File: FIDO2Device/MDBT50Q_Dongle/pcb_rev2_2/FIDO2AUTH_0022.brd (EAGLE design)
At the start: 19.5 x 34.3 mm, 40 parts, among them CN1 TE-1734028, CN2 IF_5PIN_H, SW1 SKRPACE010, SW2 SKTADAE010, U1 MDBT50Q-P1M, U2 XC6206P302MR-G, U4 RV-3028-C7, X1 NX3215SA-32.768K

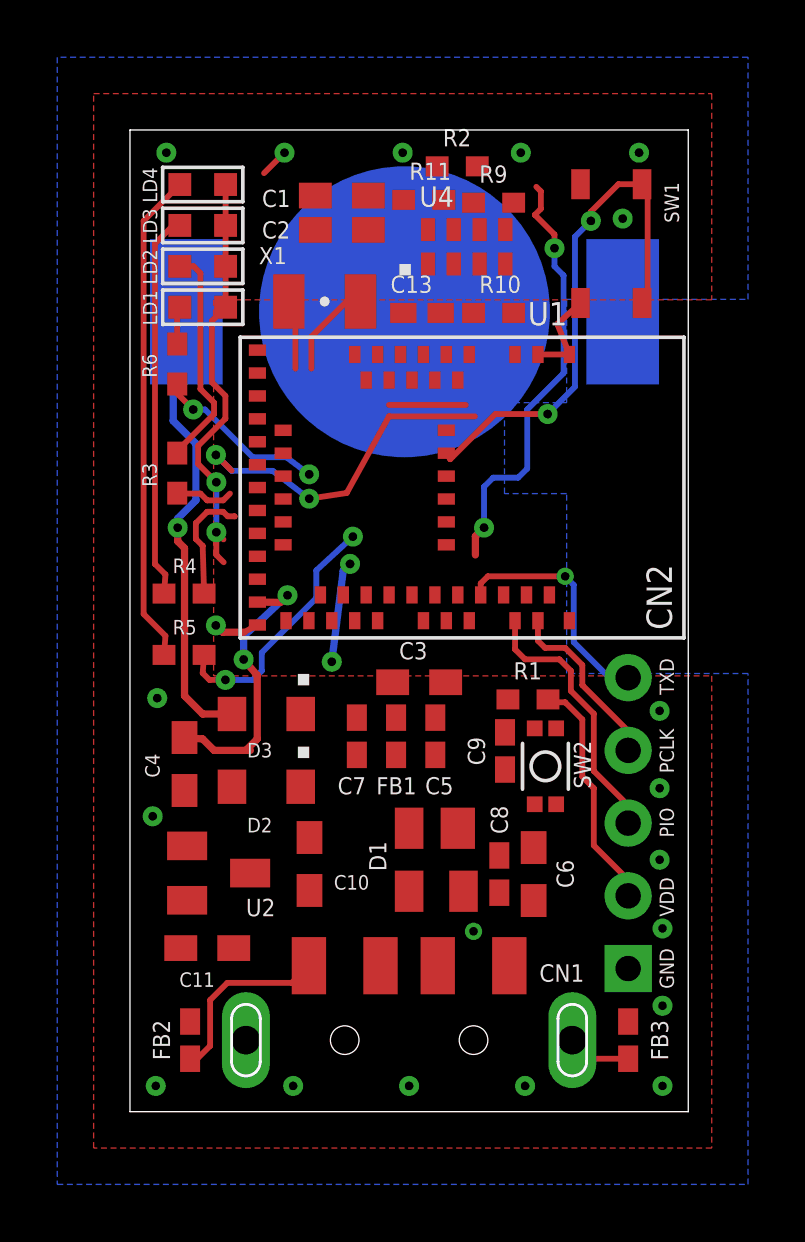
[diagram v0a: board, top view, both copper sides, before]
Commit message: 配線レイアウトを作成
・LED／RTCC／クリスタルを仮配置・配線
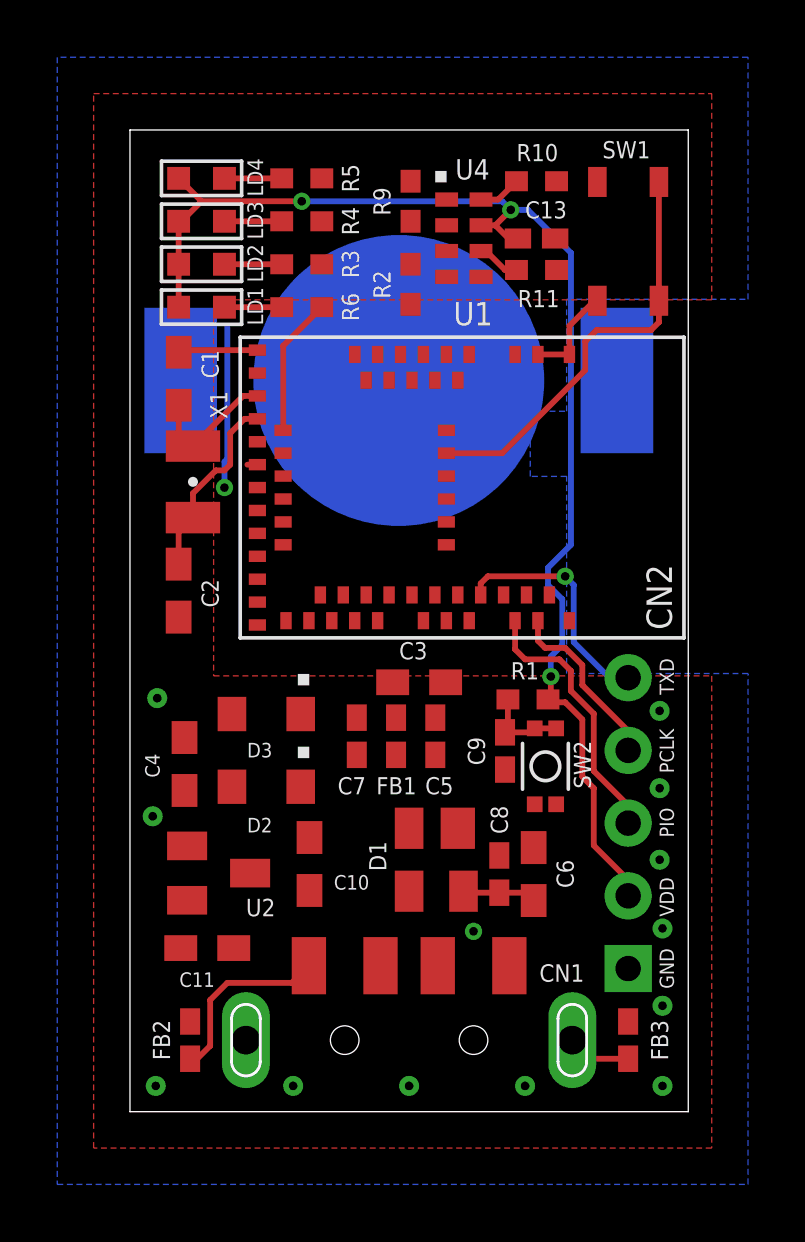
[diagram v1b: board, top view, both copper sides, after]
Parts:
- moved R5 17.1 mm to (6.00, 32.6)
- moved C2 13.8 mm to (1.70, 18.2), turned to 270 degrees
- moved R4 13.6 mm to (6.00, 31.1)
- moved C1 8.57 mm to (1.70, 25.6), turned to 90 degrees
- moved R3 8.49 mm to (6.00, 29.6), turned to 180 degrees
- moved X1 7.80 mm to (2.20, 22.0), turned to 270 degrees
- moved R10 4.84 mm to (14.2, 32.5), turned to 180 degrees
- moved R6 4.78 mm to (6.00, 28.1), turned to 180 degrees
- moved C13 4.77 mm to (14.2, 30.5)
- moved R11 4.64 mm to (14.2, 29.4), turned to 180 degrees
- moved R2 4.43 mm to (9.80, 28.9), turned to 270 degrees
- moved U4 2.94 mm to (10.7, 32.1), turned to 270 degrees
- moved R9 2.90 mm to (9.80, 31.8), turned to 90 degrees
- moved BAT1 2.41 mm to (9.39, 25.5)
- moved SW1 0.59 mm to (17.4, 30.4)
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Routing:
- net N$1: track 17.3 -> 2.00 mm
- net N$5: track 16.6 -> 2.10 mm, vias 1 -> 0
- net N$6: track 13.5 -> 2.00 mm
- net VBUS_NRF: track 10.0 -> 0.00 mm, vias 2 -> 0
- net LED4: track 8.97 -> 0.00 mm, vias 2 -> 0
- net TWI_SDA: track 12.0 -> 5.99 mm, vias 2 -> 1
- net N$7: track 7.83 -> 2.00 mm
- net LED3: track 4.15 -> 0.00 mm
- net SW1: track 18.5 -> 14.8 mm, vias 2 -> 0
- net VDD_NRF: track 42.4 -> 45.8 mm, vias 6 -> 3
- net XL2: track 3.35 -> 6.65 mm
- net RESET: track 0.00 -> 3.04 mm
- net TWI_SCL: track 2.68 -> 0.00 mm
- net VBUS: track 0.00 -> 2.58 mm
- net LED2: track 2.04 -> 0.00 mm
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
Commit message: 配線レイアウトを作成
・VBUS周りを配線
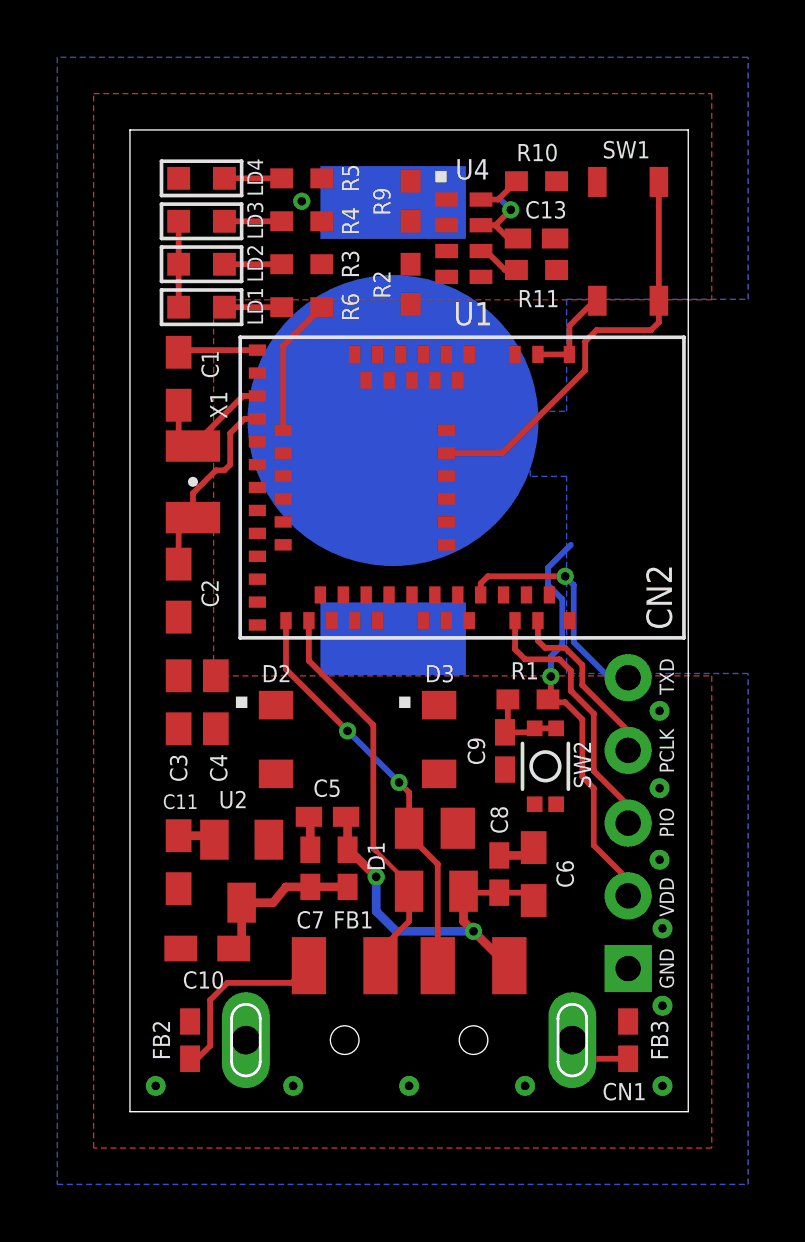
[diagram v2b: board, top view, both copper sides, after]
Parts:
- moved C3 8.43 mm to (1.70, 14.3), turned to 270 degrees
- moved D3 6.10 mm to (10.8, 13.0), turned to 270 degrees
- moved FB1 4.91 mm to (7.60, 8.50)
- moved C7 4.89 mm to (6.30, 8.50)
- moved C5 4.70 mm to (6.90, 10.3), turned to 180 degrees
- moved C10 4.63 mm to (2.70, 5.70), turned to 180 degrees
- moved C11 3.16 mm to (1.70, 8.71), turned to 270 degrees
- moved C4 2.42 mm to (3.00, 14.3)
- moved D2 1.68 mm to (5.10, 13.0), turned to 270 degrees
- moved BAT1 1.41 mm to (9.19, 24.1), turned to 90 degrees
- moved U2 0.81 mm to (3.90, 8.40), turned to 180 degrees
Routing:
- net VDD_NRF: track 45.8 -> 20.2 mm
- net D_N: track 0.00 -> 14.2 mm, vias 0 -> 2
- net D_P: track 0.00 -> 13.9 mm
- net VBUS: track 2.58 -> 13.3 mm, vias 1 -> 2
- net TWI_SDA: track 5.99 -> 0.00 mm, vias 1 -> 0
- net VBUS_NRF: track 0.00 -> 5.67 mm
- net 0V: track 6.22 -> 8.70 mm, vias 12 -> 10
- net N$5: track 2.10 -> 0.00 mm
- net N$4: track 0.00 -> 1.31 mm

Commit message: 配線レイアウトを作成
・VDD_NRF周りを配線
・RESET配線を修正
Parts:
- moved R1 0.10 mm to (13.8, 14.4)
- turned BAT1 to 270 degrees
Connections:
- net N$5: now also BAT1.+@2; no longer BAT1.+@1
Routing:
- net VDD_NRF: track 20.2 -> 66.7 mm, vias 3 -> 7
- net RESET: track 3.04 -> 16.5 mm, vias 0 -> 2
- net N$5: track 0.00 -> 5.97 mm, vias 0 -> 1
- net VBUS_NRF: track 5.67 -> 9.11 mm
- net 0V: track 8.70 -> 9.75 mm, vias 10 -> 11

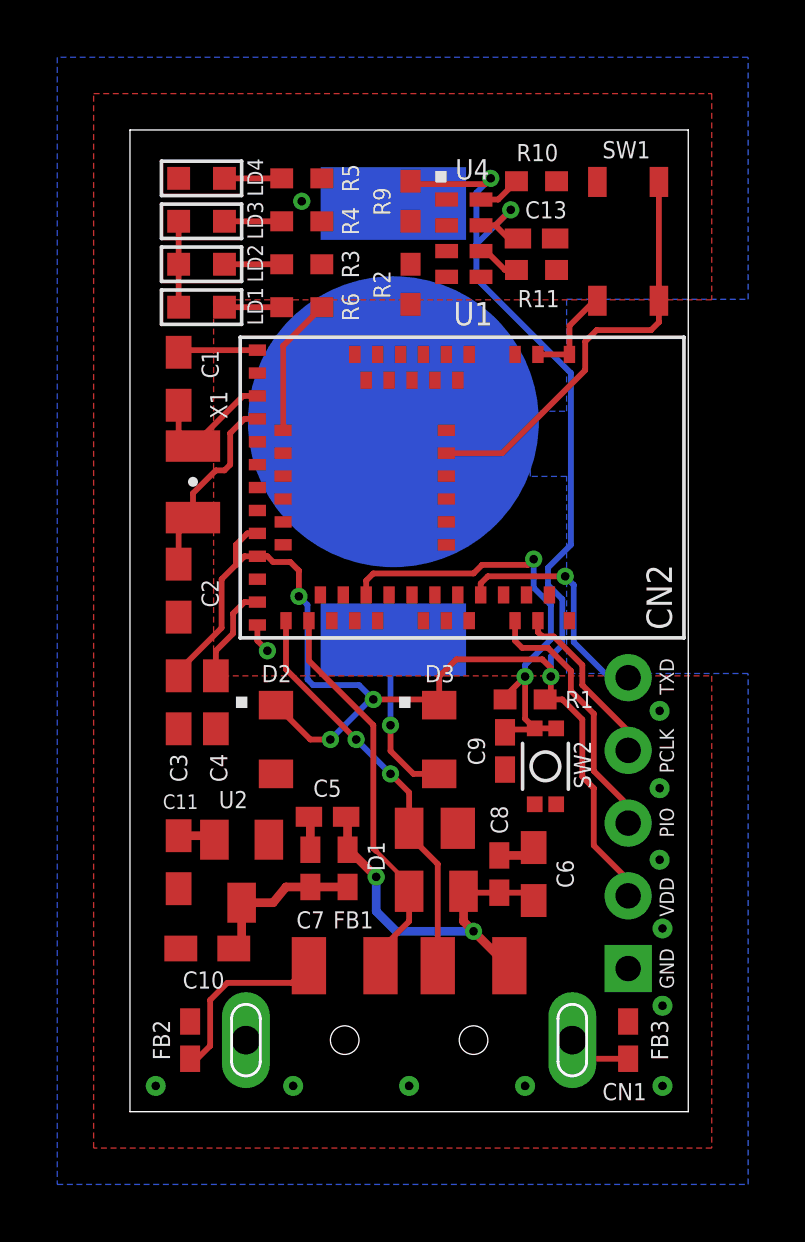
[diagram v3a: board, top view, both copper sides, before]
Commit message: 配線レイアウトを作成
・基板下半分のVDD_NRF、VBUS_NRFの配線を確定
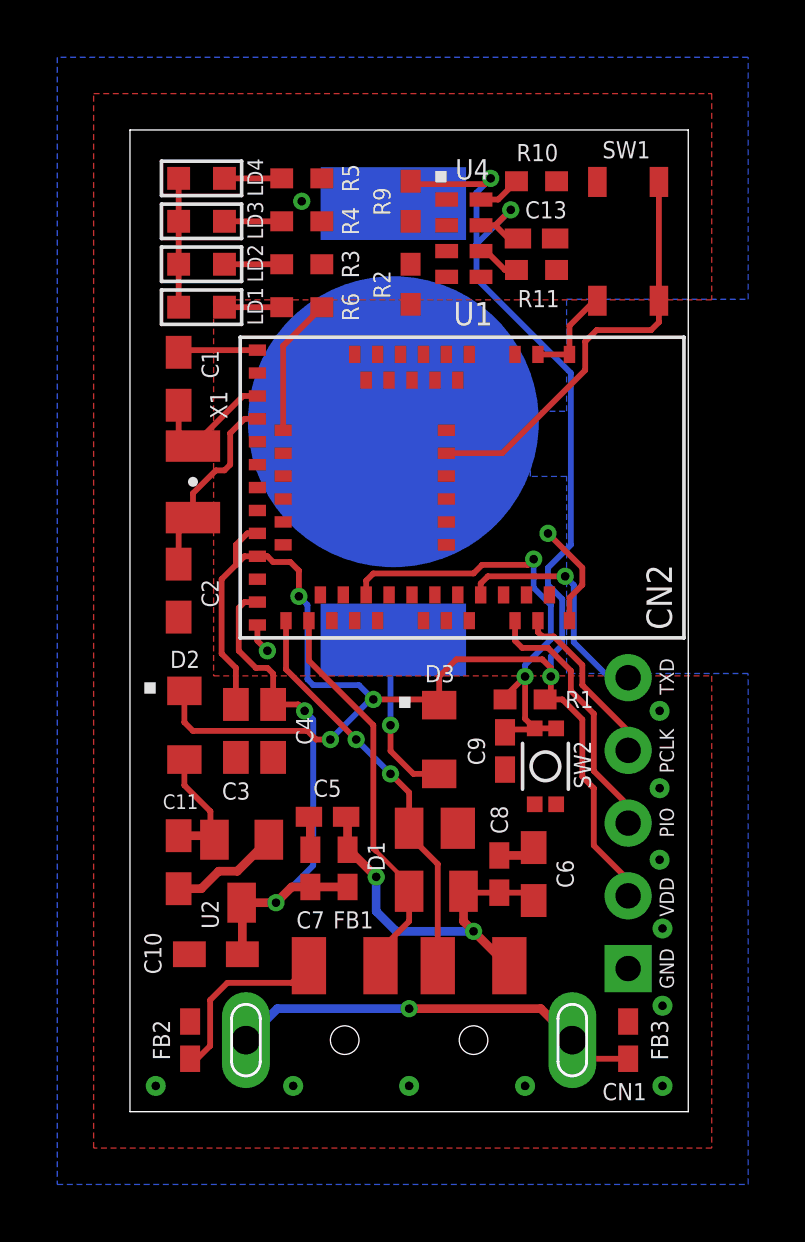
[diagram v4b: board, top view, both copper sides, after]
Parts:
- moved D2 3.24 mm to (1.90, 13.5)
- moved C3 2.24 mm to (3.70, 13.3)
- moved C4 2.24 mm to (5.00, 13.3)
- moved C10 0.36 mm to (3.00, 5.50)
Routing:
- net N$3: track 2.22 -> 14.5 mm, vias 0 -> 1
- net VBUS_NRF: track 9.11 -> 19.4 mm, vias 0 -> 2
- net 0V: track 9.75 -> 17.3 mm, vias 11 -> 12
- net VDD_NRF: track 66.7 -> 72.8 mm
- net N$4: track 1.31 -> 4.35 mm
